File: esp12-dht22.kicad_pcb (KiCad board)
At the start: 2 copper layers, 4 parts

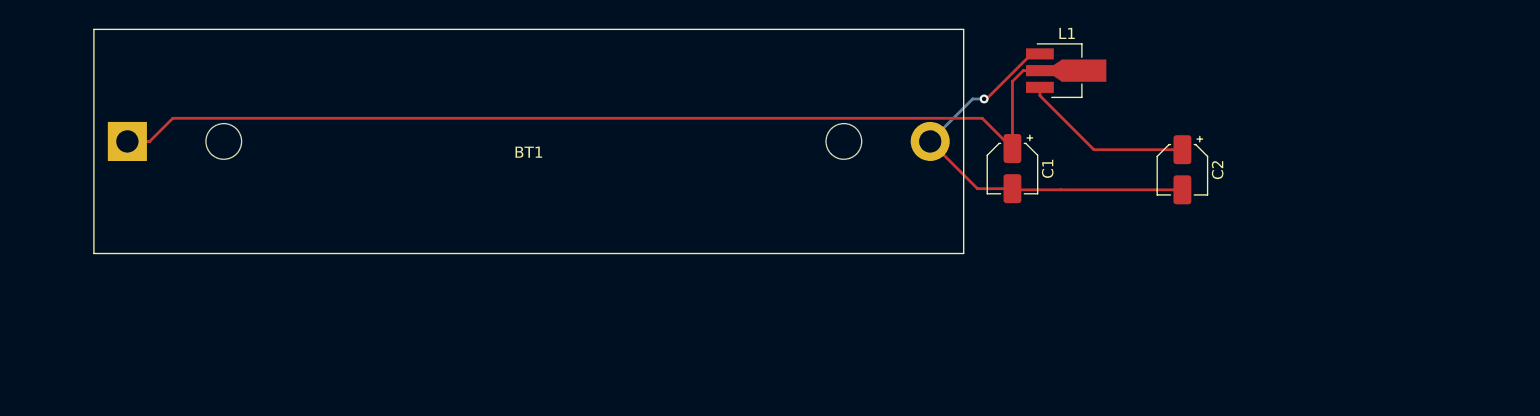
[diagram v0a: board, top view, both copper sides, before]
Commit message: added esp, dht22 and battery voltage divider for adc
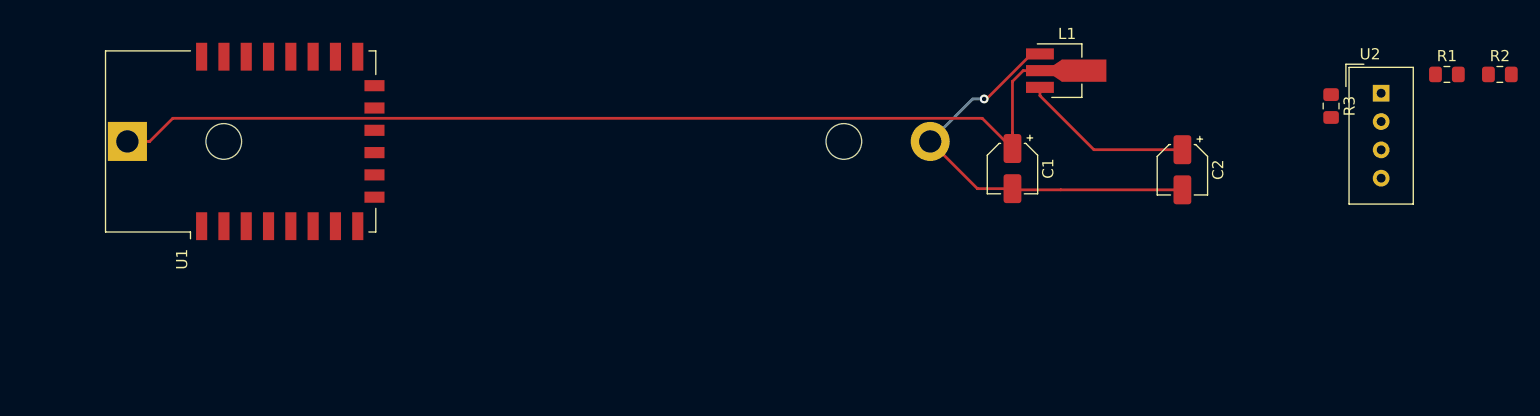
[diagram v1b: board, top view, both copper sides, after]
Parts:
- added R1: 330k, Resistor_SMD:R_0805_2012Metric_Pad1.15x1.40mm_HandSolder, F.Cu at (195.8, 90.5)
- added R2: 100k, Resistor_SMD:R_0805_2012Metric_Pad1.15x1.40mm_HandSolder, F.Cu at (200.6, 90.5)
- added R3: 4k7, Resistor_SMD:R_0805_2012Metric_Pad1.15x1.40mm_HandSolder, F.Cu at (185.4, 93.3)
- added U1: ESP-12E, RF_Module:ESP-12E, F.Cu at (87.6, 96.5)
- added U2: DHT22, Sensor:Aosong_DHT11_5.5x12.0_P2.54mm, F.Cu at (189.9, 92.2)
- BT1: moved to B.Cu

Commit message: changed data pin from gpio5 to gpio4
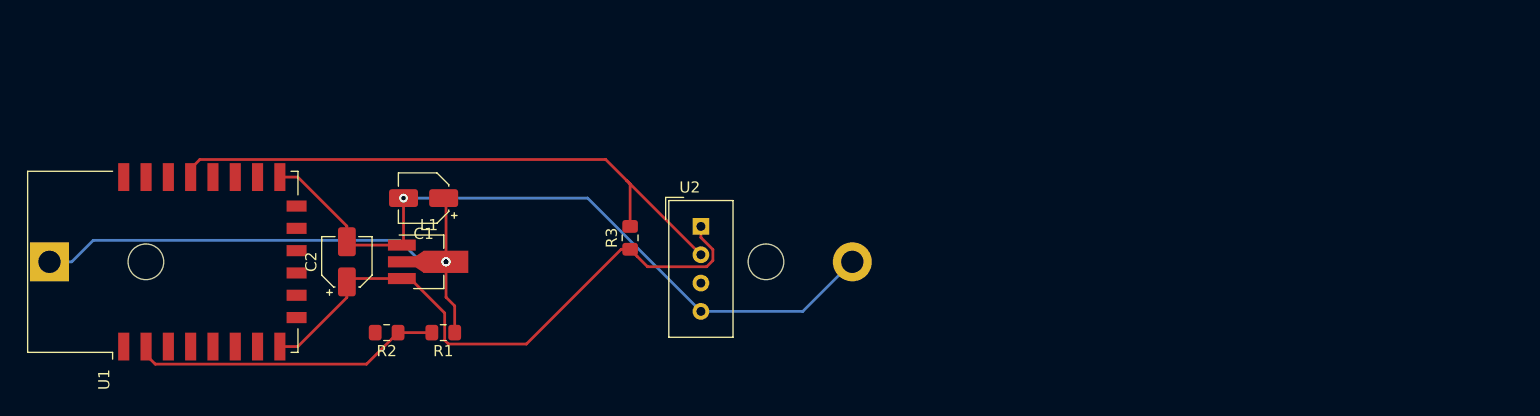
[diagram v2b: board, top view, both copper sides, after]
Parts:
- moved R2 102.5 mm to (100.7, 113.7), turned to 180 degrees
- moved R1 92.9 mm to (105.8, 113.7), turned to 180 degrees
- moved C2 75.4 mm to (97.2, 107.3), turned to 90 degrees
- moved R3 64.0 mm to (122.6, 105.2), turned to 90 degrees
- moved U2 62.2 mm to (128.9, 104.1)
- moved L1 59.7 mm to (104.1, 107.3)
- moved C1 52.9 mm to (104.0, 101.6), turned to 180 degrees
- moved BT1 12.9 mm to (70.5, 107.3)
- moved U1 12.9 mm to (80.6, 107.3)
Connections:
- U1 pad 19: Net-(U1-Pad19) -> DHT_Data
- U1 pad 20: DHT_Data -> Net-(U1-Pad20)
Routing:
- net DHT_Data: track 0.00 -> 54.6 mm
- net +BATT: track 90.2 -> 49.6 mm, vias 0 -> 3
- net VCC: track 15.5 -> 54.0 mm
- net ADC: track 0.00 -> 27.9 mm
- net GND: track 37.5 -> 64.9 mm

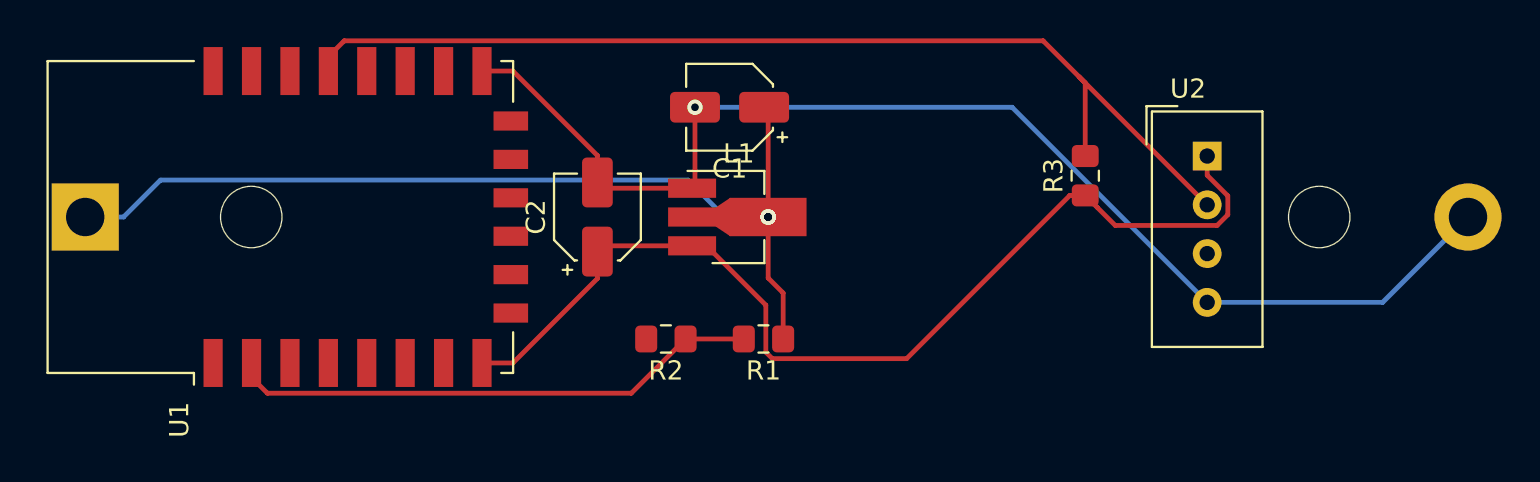
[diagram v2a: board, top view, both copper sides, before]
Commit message: added 100nF caps
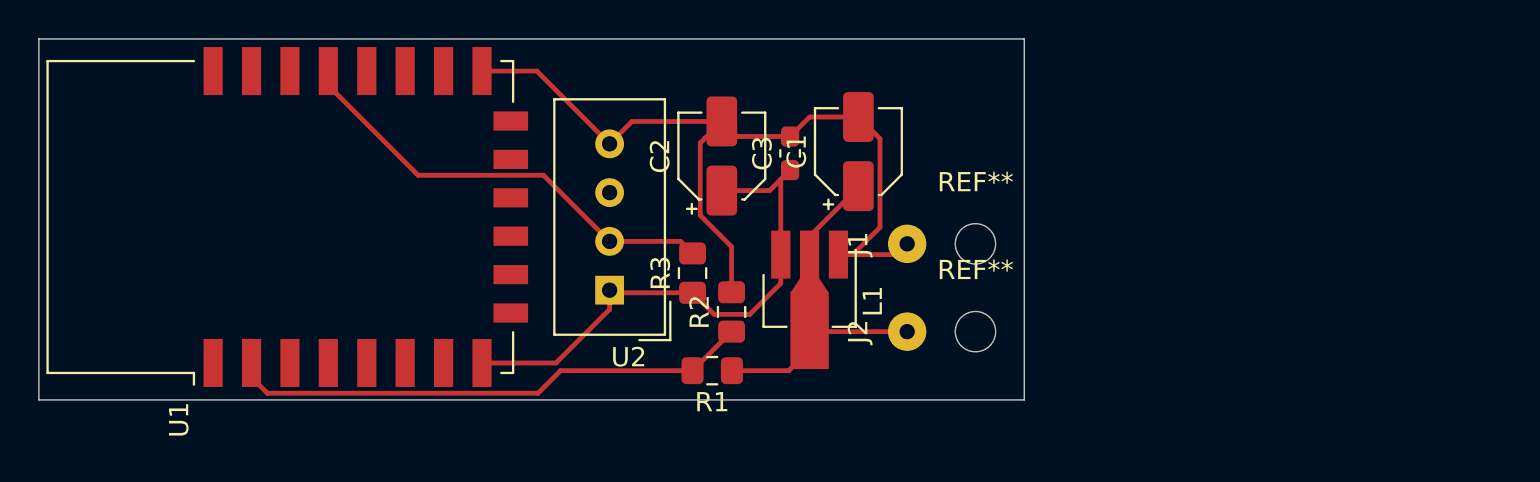
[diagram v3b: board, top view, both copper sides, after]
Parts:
- removed BT1: Battery_Cell, Battery:BatteryHolder_MPD_BH-18650-PC2
- added C3: 100nF, Capacitor_SMD:C_0603_1608Metric_Pad1.05x0.95mm_HandSolder, F.Cu at (107.2, 104.0)
- added J1: BAT-, Connector_Wire:SolderWirePad_1x01_Drill0.8mm, F.Cu at (113.3, 108.7)
- added J2: BAT+, Connector_Wire:SolderWirePad_1x01_Drill0.8mm, F.Cu at (113.3, 113.3)
- added REF**: MountingHole_2.1mm, MountingHole:MountingHole_2.1mm, F.Cu at (116.8, 113.3)
- added REF**: MountingHole_2.1mm, MountingHole:MountingHole_2.1mm, F.Cu at (116.8, 108.7)
- moved U2 31.9 mm to (97.8, 111.1), turned to 180 degrees
- moved R3 21.1 mm to (102.1, 110.2)
- moved C2 7.21 mm to (103.6, 104.1)
- moved C1 7.09 mm to (110.7, 103.9), turned to 90 degrees
- moved L1 5.71 mm to (108.2, 111.3), turned to 270 degrees
- moved R2 3.70 mm to (104.1, 112.3), turned to 90 degrees
- moved R1 3.14 mm to (103.1, 115.3)
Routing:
- net DHT_Data: track 54.6 -> 23.3 mm
- net +BATT: track 49.6 -> 19.3 mm, vias 3 -> 0
- net VCC: track 54.0 -> 29.0 mm
- net GND: track 64.9 -> 45.2 mm, vias 1 -> 0
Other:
- board outline added: 51.3 x 18.8 mm

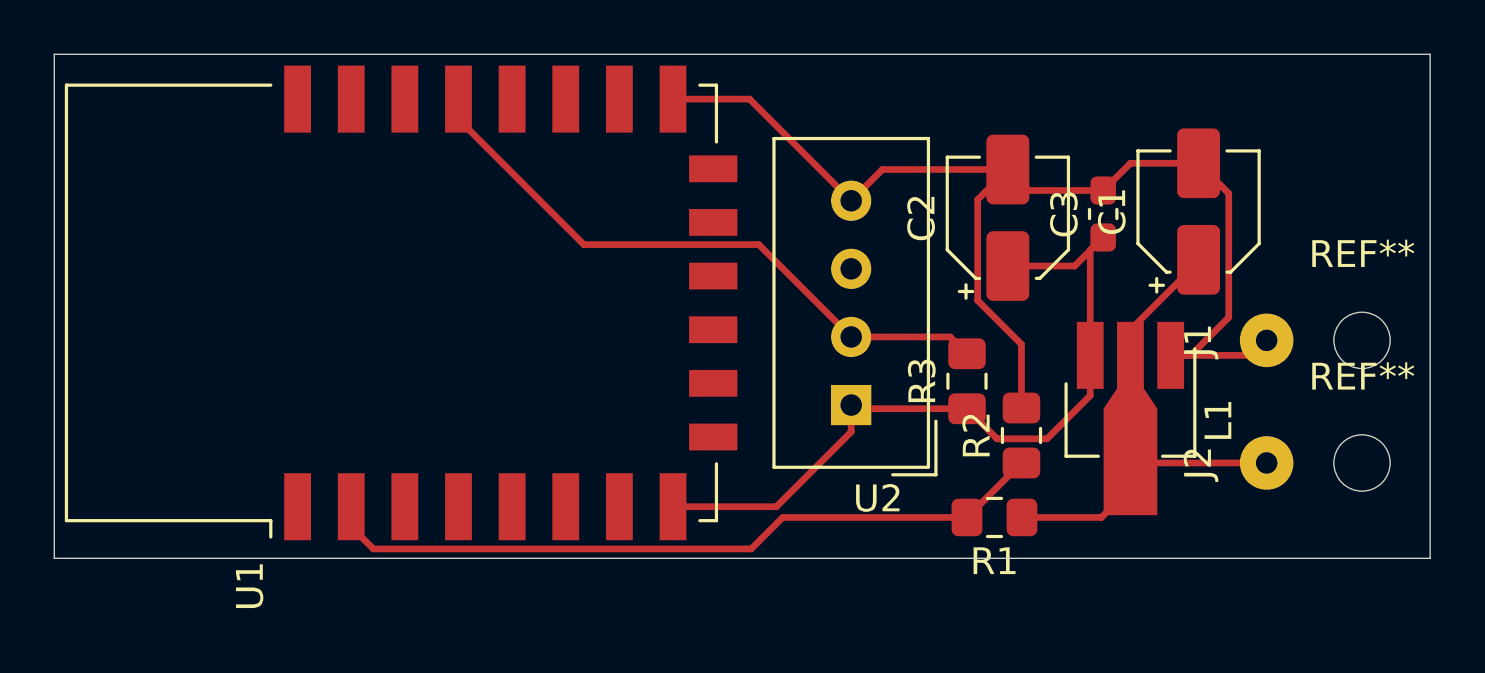
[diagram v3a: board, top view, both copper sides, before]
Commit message: added JST PH connector for battery
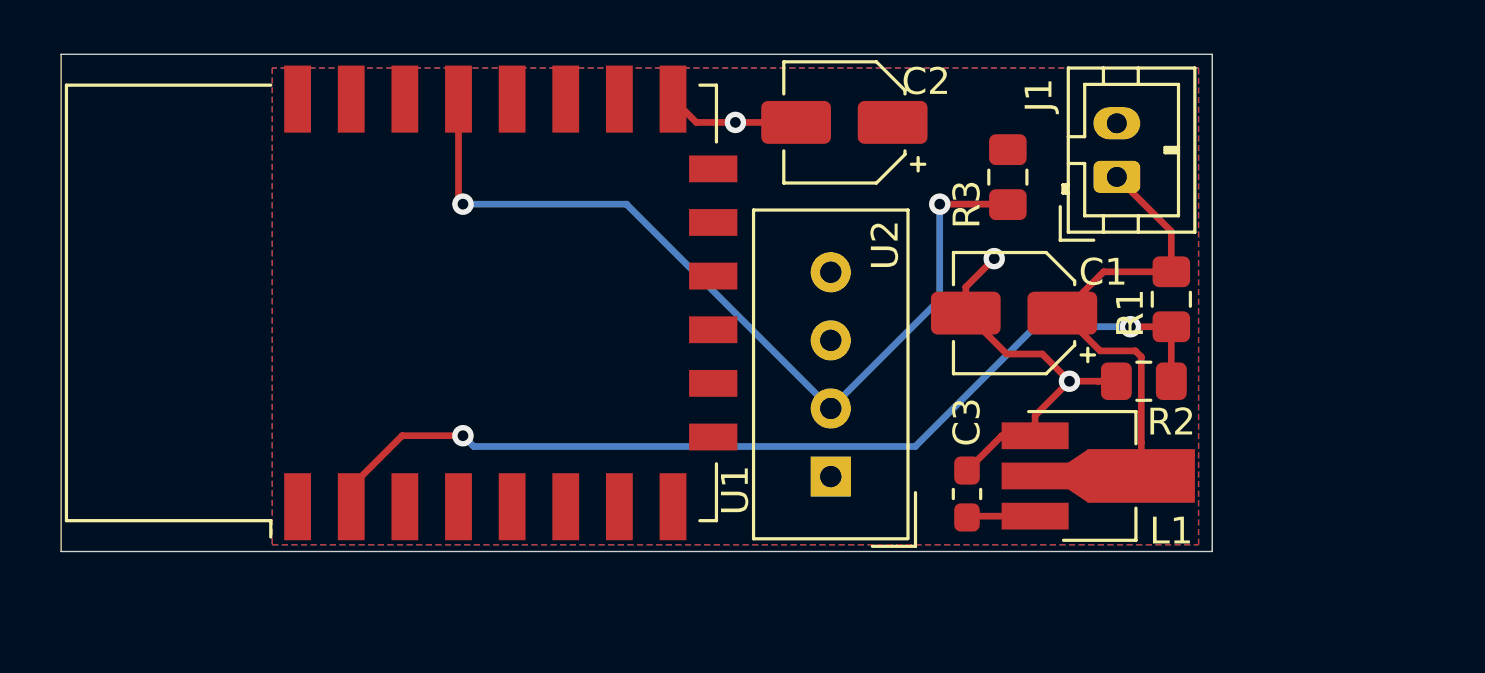
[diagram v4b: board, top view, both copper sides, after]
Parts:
- removed J2: BAT+, Connector_Wire:SolderWirePad_1x01_Drill0.8mm
- removed the REF** at (116.8, 113.3)
- removed the REF** at (116.8, 108.7)
- added REF**: KiCad-Logo2_5mm_SilkScreen, Symbol:KiCad-Logo2_5mm_SilkScreen, B.Cu at (72.1, 107.2)
- J1: value BAT- -> Battery; footprint Connector_Wire:SolderWirePad_1x01_Drill0.8mm -> Connector_JST:JST_PH_B2B-PH-K_1x02_P2.00mm_Vertical
- moved C3 11.6 mm to (102.1, 114.4)
- moved R1 10.5 mm to (109.7, 107.2), turned to 270 degrees
- moved J1 8.27 mm to (107.7, 102.6)
- moved C1 7.85 mm to (103.9, 107.7), turned to 180 degrees
- moved R3 7.76 mm to (103.6, 102.6), turned to 270 degrees
- moved C2 7.06 mm to (97.5, 100.6), turned to 180 degrees
- moved R2 4.99 mm to (108.7, 110.2), turned to 180 degrees
- moved L1 2.97 mm to (106.6, 113.8), turned to 0 degrees
- moved U2 2.77 mm to (97.0, 113.8)
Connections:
- J1 pad 1: GND -> +BATT
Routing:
- net VCC: track 29.0 -> 2.56 mm
- net GND: track 45.2 -> 19.7 mm, vias 0 -> 3
- net DHT_Data: track 23.3 -> 32.7 mm, vias 0 -> 2
- net ADC: track 27.4 -> 36.2 mm, vias 0 -> 2
- net +BATT: track 19.3 -> 21.1 mm
- added copper zone on B.Cu, net GND
- added copper zone on F.Cu, net VCC
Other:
- board size 51.3 x 18.8 mm -> 42.9 x 18.5 mm

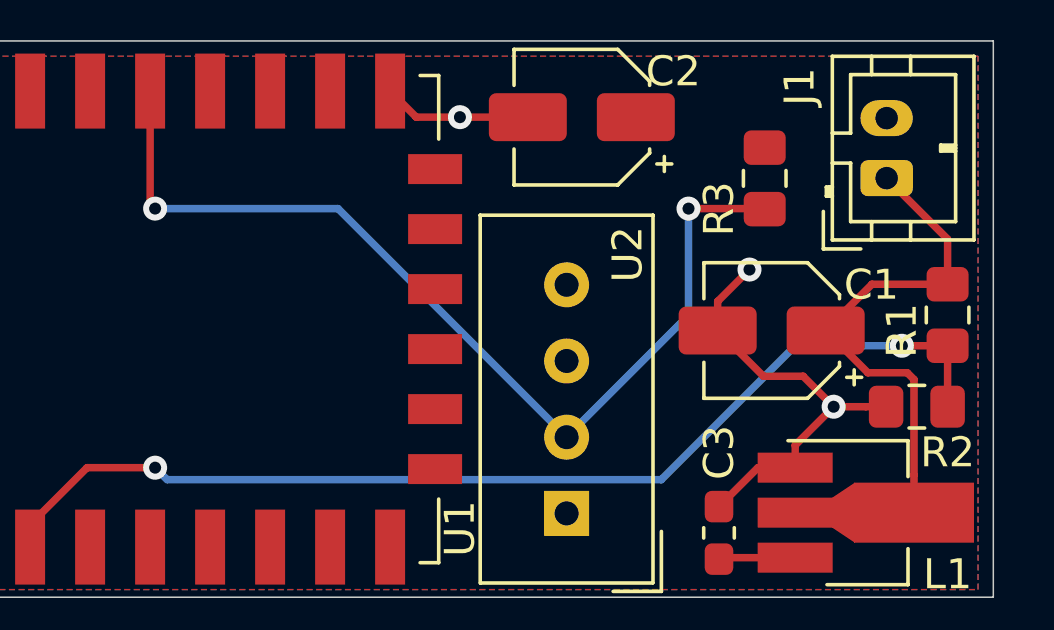
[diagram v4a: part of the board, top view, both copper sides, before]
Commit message: moved via and added date to bottom silkscreen
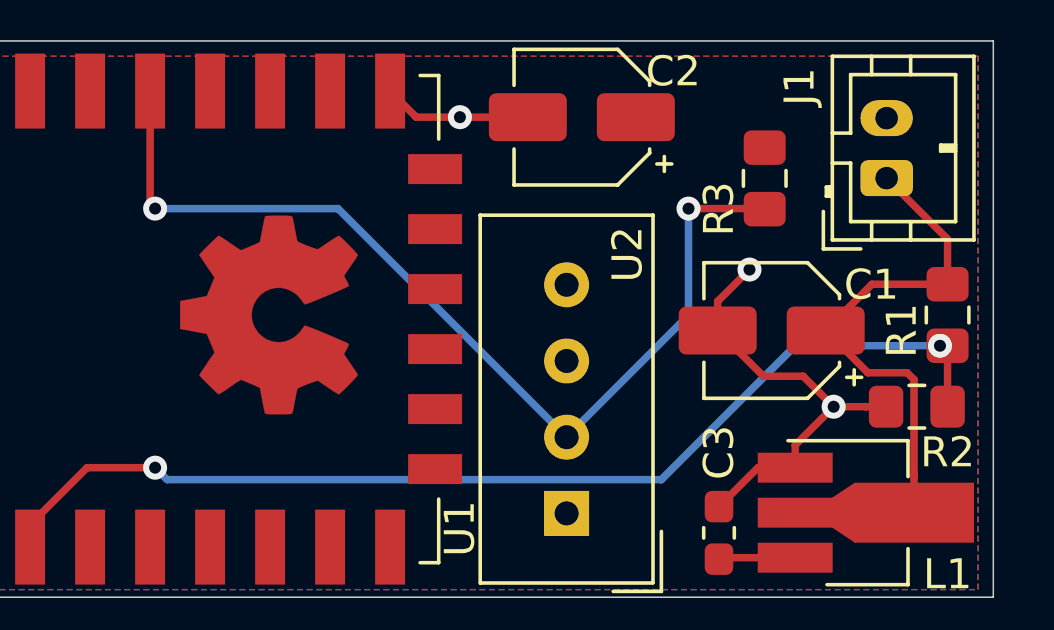
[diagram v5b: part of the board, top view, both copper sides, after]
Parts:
- added REF**: OSHW-Symbol_6.7x6mm_Copper, Symbol:OSHW-Symbol_6.7x6mm_Copper, F.Cu at (87.1, 107.2)
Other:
- board text added: "-+"
- board text added: "BAT"
- board text added: "Dr.Bock 07/2019"
